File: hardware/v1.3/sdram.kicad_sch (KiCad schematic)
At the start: 10 parts, among them U1 ECP5-CABGA256, U11 W9825G6KH

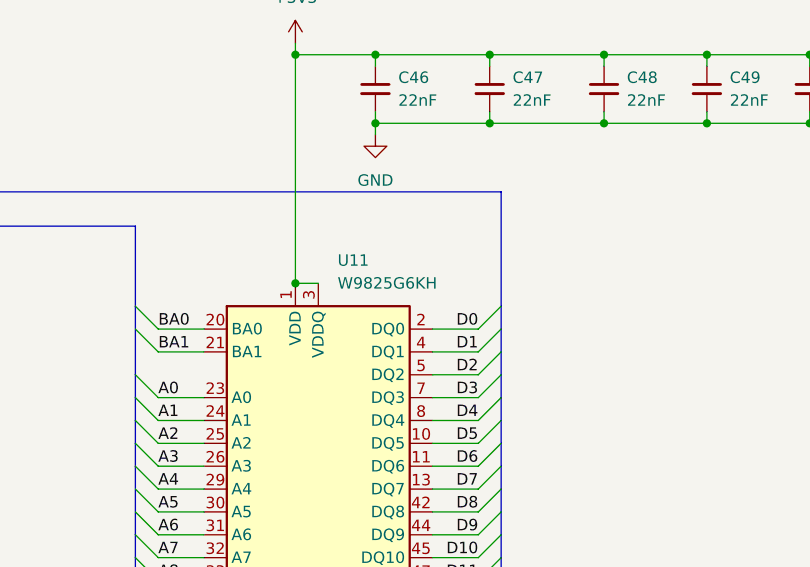
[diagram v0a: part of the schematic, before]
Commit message: Replaced memory AS4C16M16SA 54-TFBGA (8x8)
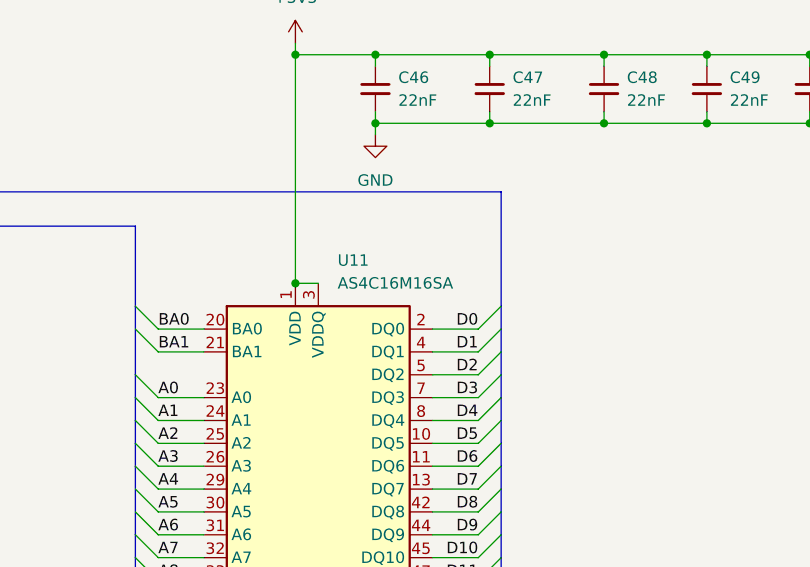
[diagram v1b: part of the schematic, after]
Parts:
- U11: value W9825G6KH -> AS4C16M16SA; footprint Package_SO:TSOP-II-54_22.2x10.16mm_P0.8mm -> Package_BGA:Alliance_TFBGA-54_8x8mm_Layout9x9_P0.8mm; LCSC Link https://lcsc.com/product-detail/SDRAM_Winbond-W9825G6KH-6_C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 -> https://www.lcsc.com/product-detail/C17570045.html?s_z=n_AS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; LCSC Part # C62246 -> C17570045; Manufactuer Part Number W9825G6KH-6 -> AS4C16M16SA-6BAN
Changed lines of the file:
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@@
 			)
 		)
-		(property "Value" "W9825G6KH"
+		(property "Value" "AS4C16M16SA"
 			(at 177.4033 64.77 0)
 			(effects
@@
 			)
 		)
-		(property "Footprint" "Package_SO:TSOP-II-54_22.2x10.16mm_P0.8mm"
+		(property "Footprint" "Package_BGA:Alliance_TFBGA-54_8x8mm_Layout9x9_P0.8mm"
 			(at 175.26 135.89 0)
 			(effects
@@
 			)
 		)
-		(property "Datasheet" "https://www.micron.com/-/media/client/global/documents/products/data-sheet/dram/256mb_sdr.pdf"
+		(property "Datasheet" "https://www.alliancememory.com/wp-content/uploads/256Mb-AS4C16M16SA-CI_V3.0_March-2015.pdf"
 			(at 175.26 106.68 0)
 			(effects
@@
 			)
 		)
-		(property "Description" "256M – (16M x 16 bit) Synchronous DRAM (SDRAM), TSOP-II-54"
+		(property "Description" "SDRAM Memory IC 256Mbit Parallel 166 MHz 5 ns 54-TFBGA (8x8)"
 			(at 175.26 100.33 0)
 			(effects
@@
 			)
 		)
-		(property "LCSC Part #" "C62246"
+		(property "LCSC Part #" "C17570045"
 			(at 175.26 100.33 0)
 			(effects
@@
 			)
 		)
-		(property "LCSC Link" "https://lcsc.com/product-detail/SDRAM_Winbond-W9825G6KH-6_C62246.html"
+		(property "LCSC Link" "https://www.lcsc.com/product-detail/C17570045.html?s_z=n_AS4C16M16SA-6BAN"
 			(at 175.26 100.33 0)
 			(effects
@@
 			)
 		)
-		(property "Manufactuer Part Number" "W9825G6KH-6"
+		(property "Manufactuer Part Number" "AS4C16M16SA-6BAN"
 			(at 175.26 100.33 0)
 			(effects
